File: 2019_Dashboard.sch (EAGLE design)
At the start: 48 parts, among them IC1 MCP23017SO, IC2 MCP23017SO, IC3 MCP23017SO, Y1 16MHz

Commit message: 11/26/18 I2C Dashboard
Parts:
- added LAUNCH, LPADDLE, PARTY1, PARTY2, RPADDLE, T/S-TOOGLE: (no value), SparkFun-Connectors:CONN_02LOCK
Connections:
- new net LAUNCH: IC2.GPB3, LAUNCH.2
- new net LPADDLE: IC2.GPB0, LPADDLE.2
- new net PARTY1: IC2.GPB4, PARTY1.2
- new net PARTY2: IC2.GPB5, PARTY2.2
- new net RPADDLE: IC2.GPB1, RPADDLE.2
- new net T/S-TOOGLE: IC2.GPB2, T/S-TOOGLE.2
- net VCC: now also LAUNCH.1, LPADDLE.1, PARTY1.1, PARTY2.1, RPADDLE.1, T/S-TOOGLE.1
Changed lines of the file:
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@@
 <part name="R12" library="SparkFun-Resistors" library_urn="urn:adsk.eagle:library:532" deviceset="330OHM" device="-0603-1/10W-1%" package3d_urn="urn:adsk.eagle:package:39650/1" value="330"/>
 <part name="GND11" library="SparkFun-PowerSymbols" library_urn="urn:adsk.eagle:library:530" deviceset="GND" device=""/>
+<part name="PARTY2" library="SparkFun-Connectors" library_urn="urn:adsk.eagle:library:513" deviceset="CONN_02" device="LOCK" package3d_urn="urn:adsk.eagle:package:38045/1"/>
+<part name="T/S-TOOGLE" library="SparkFun-Connectors" library_urn="urn:adsk.eagle:library:513" deviceset="CONN_02" device="LOCK" package3d_urn="urn:adsk.eagle:package:38045/1"/>
+<part name="RPADDLE" library="SparkFun-Connectors" library_urn="urn:adsk.eagle:library:513" deviceset="CONN_02" device="LOCK" package3d_urn="urn:adsk.eagle:package:38045/1"/>
+<part name="PARTY1" library="SparkFun-Connectors" library_urn="urn:adsk.eagle:library:513" deviceset="CONN_02" device="LOCK" package3d_urn="urn:adsk.eagle:package:38045/1"/>
+<part name="LAUNCH" library="SparkFun-Connectors" library_urn="urn:adsk.eagle:library:513" deviceset="CONN_02" device="LOCK" package3d_urn="urn:adsk.eagle:package:38045/1"/>
+<part name="LPADDLE" library="SparkFun-Connectors" library_urn="urn:adsk.eagle:library:513" deviceset="CONN_02" device="LOCK" package3d_urn="urn:adsk.eagle:package:38045/1"/>
+<part name="SUPPLY2" library="SparkFun-PowerSymbols" library_urn="urn:adsk.eagle:library:530" deviceset="VCC" device=""/>
+<part name="SUPPLY3" library="SparkFun-PowerSymbols" library_urn="urn:adsk.eagle:library:530" deviceset="VCC" device=""/>
+<part name="SUPPLY4" library="SparkFun-PowerSymbols" library_urn="urn:adsk.eagle:library:530" deviceset="VCC" device=""/>
+<part name="SUPPLY5" library="SparkFun-PowerSymbols" library_urn="urn:adsk.eagle:library:530" deviceset="VCC" device=""/>
+<part name="SUPPLY6" library="SparkFun-PowerSymbols" library_urn="urn:adsk.eagle:library:530" deviceset="VCC" device=""/>
+<part name="SUPPLY7" library="SparkFun-PowerSymbols" library_urn="urn:adsk.eagle:library:530" deviceset="VCC" device=""/>
 </parts>
 <sheets>
@@
 <instance part="R12" gate="G$1" x="78.74" y="-88.9"/>
 <instance part="GND11" gate="1" x="104.14" y="-104.14"/>
+<instance part="PARTY2" gate="G$1" x="-45.72" y="172.72" rot="R180"/>
+<instance part="T/S-TOOGLE" gate="G$1" x="-45.72" y="157.48" rot="R180"/>
+<instance part="RPADDLE" gate="G$1" x="-45.72" y="139.7" rot="R180"/>
+<instance part="PARTY1" gate="G$1" x="-71.12" y="172.72" rot="R180"/>
+<instance part="LAUNCH" gate="G$1" x="-71.12" y="157.48" rot="R180"/>
+<instance part="LPADDLE" gate="G$1" x="-71.12" y="139.7" rot="R180"/>
+<instance part="SUPPLY2" gate="G$1" x="-88.9" y="180.34"/>
+<instance part="SUPPLY3" gate="G$1" x="-60.96" y="182.88"/>
+<instance part="SUPPLY4" gate="G$1" x="-88.9" y="165.1"/>
+<instance part="SUPPLY5" gate="G$1" x="-60.96" y="165.1"/>
+<instance part="SUPPLY6" gate="G$1" x="-60.96" y="147.32"/>
+<instance part="SUPPLY7" gate="G$1" x="-88.9" y="147.32"/>
 </instances>
 <busses>
@@
 <junction x="-15.24" y="129.54"/>
 </segment>
+<segment>
+<pinref part="PARTY1" gate="G$1" pin="1"/>
+<wire x1="-78.74" y1="172.72" x2="-88.9" y2="172.72" width="0.1524" layer="91"/>
+<wire x1="-88.9" y1="172.72" x2="-88.9" y2="180.34" width="0.1524" layer="91"/>
+<pinref part="SUPPLY2" gate="G$1" pin="VCC"/>
+</segment>
+<segment>
+<pinref part="PARTY2" gate="G$1" pin="1"/>
+<wire x1="-53.34" y1="172.72" x2="-60.96" y2="172.72" width="0.1524" layer="91"/>
+<wire x1="-60.96" y1="172.72" x2="-60.96" y2="182.88" width="0.1524" layer="91"/>
+<pinref part="SUPPLY3" gate="G$1" pin="VCC"/>
+</segment>
+<segment>
+<pinref part="LAUNCH" gate="G$1" pin="1"/>
+<wire x1="-78.74" y1="157.48" x2="-88.9" y2="157.48" width="0.1524" layer="91"/>
+<wire x1="-88.9" y1="157.48" x2="-88.9" y2="165.1" width="0.1524" layer="91"/>
+<pinref part="SUPPLY4" gate="G$1" pin="VCC"/>
+</segment>
+<segment>
+<pinref part="T/S-TOOGLE" gate="G$1" pin="1"/>
+<wire x1="-53.34" y1="157.48" x2="-60.96" y2="157.48" width="0.1524" layer="91"/>
+<wire x1="-60.96" y1="157.48" x2="-60.96" y2="165.1" width="0.1524" layer="91"/>
+<pinref part="SUPPLY5" gate="G$1" pin="VCC"/>
+</segment>
+<segment>
+<pinref part="RPADDLE" gate="G$1" pin="1"/>
+<wire x1="-53.34" y1="139.7" x2="-60.96" y2="139.7" width="0.1524" layer="91"/>
+<wire x1="-60.96" y1="139.7" x2="-60.96" y2="147.32" width="0.1524" layer="91"/>
+<pinref part="SUPPLY6" gate="G$1" pin="VCC"/>
+</segment>
+<segment>
+<pinref part="LPADDLE" gate="G$1" pin="1"/>
+<wire x1="-78.74" y1="139.7" x2="-88.9" y2="139.7" width="0.1524" layer="91"/>
+<wire x1="-88.9" y1="139.7" x2="-88.9" y2="147.32" width="0.1524" layer="91"/>
+<pinref part="SUPPLY7" gate="G$1" pin="VCC"/>
+</segment>
 </net>
 <net name="OSC1" class="0">
@@
 </segment>
 </net>
+<net name="RPADDLE" class="0">
+<segment>
+<pinref part="RPADDLE" gate="G$1" pin="2"/>
+<wire x1="-53.34" y1="137.16" x2="-53.34" y2="132.08" width="0.1524" layer="91"/>
+<wire x1="-53.34" y1="132.08" x2="-63.5" y2="132.08" width="0.1524" layer="91"/>
+<label x="-63.5" y="127" size="1.778" layer="95"/>
+</segment>
+<segment>
+<pinref part="IC2" gate="G$1" pin="GPB1"/>
+<wire x1="17.78" y1="45.72" x2="33.02" y2="45.72" width="0.1524" layer="91"/>
+<label x="25.4" y="45.72" size="1.778" layer="95"/>
+</segment>
+</net>
+<net name="LPADDLE" class="0">
+<segment>
+<pinref part="LPADDLE" gate="G$1" pin="2"/>
+<wire x1="-78.74" y1="137.16" x2="-78.74" y2="132.08" width="0.1524" layer="91"/>
+<wire x1="-78.74" y1="132.08" x2="-88.9" y2="132.08" width="0.1524" layer="91"/>
+<label x="-86.36" y="127" size="1.778" layer="95"/>
+</segment>
+<segment>
+<pinref part="IC2" gate="G$1" pin="GPB0"/>
+<wire x1="17.78" y1="48.26" x2="33.02" y2="48.26" width="0.1524" layer="91"/>
+<label x="25.4" y="48.26" size="1.778" layer="95"/>
+</segment>
+</net>
+<net name="LAUNCH" class="0">
+<segment>
+<pinref part="LAUNCH" gate="G$1" pin="2"/>
+<wire x1="-78.74" y1="154.94" x2="-78.74" y2="149.86" width="0.1524" layer="91"/>
+<label x="-81.28" y="149.86" size="1.778" layer="95"/>
+</segment>
+<segment>
+<pinref part="IC2" gate="G$1" pin="GPB3"/>
+<wire x1="17.78" y1="40.64" x2="33.02" y2="40.64" width="0.1524" layer="91"/>
+<label x="25.4" y="40.64" size="1.778" layer="95"/>
+</segment>
+</net>
+<net name="T/S-TOOGLE" class="0">
+<segment>
+<pinref part="T/S-TOOGLE" gate="G$1" pin="2"/>
+<wire x1="-53.34" y1="154.94" x2="-60.96" y2="154.94" width="0.1524" layer="91"/>
+<label x="-58.42" y="160.02" size="1.778" layer="95"/>
+</segment>
+<segment>
+<pinref part="IC2" gate="G$1" pin="GPB2"/>
+<wire x1="17.78" y1="43.18" x2="33.02" y2="43.18" width="0.1524" layer="91"/>
+<label x="25.4" y="43.18" size="1.778" layer="95"/>
+</segment>
+</net>
+<net name="PARTY1" class="0">
+<segment>
+<pinref part="PARTY1" gate="G$1" pin="2"/>
+<wire x1="-78.74" y1="170.18" x2="-86.36" y2="170.18" width="0.1524" layer="91"/>
+<label x="-86.36" y="170.18" size="1.778" layer="95"/>
+</segment>
+<segment>
+<pinref part="IC2" gate="G$1" pin="GPB4"/>
+<wire x1="17.78" y1="38.1" x2="33.02" y2="38.1" width="0.1524" layer="91"/>
+<label x="25.4" y="38.1" size="1.778" layer="95"/>
+</segment>
+</net>
+<net name="PARTY2" class="0">
+<segment>
+<pinref part="PARTY2" gate="G$1" pin="2"/>
+<wire x1="-53.34" y1="170.18" x2="-60.96" y2="170.18" width="0.1524" layer="91"/>
+<label x="-60.96" y="170.18" size="1.778" layer="95"/>
+</segment>
+<segment>
+<pinref part="IC2" gate="G$1" pin="GPB5"/>
+<wire x1="17.78" y1="35.56" x2="35.56" y2="35.56" width="0.1524" layer="91"/>
+<label x="25.4" y="35.56" size="1.778" layer="95"/>
+</segment>
+</net>

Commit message: Yeet a few pins
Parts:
- removed IC2: MCP23017SO, adafruit:MCP23017SO
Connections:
- removed net N$16: IC2.GPA1, U$1.B
- removed net N$17: IC2.GPA2, U$1.C
- removed net N$18: IC2.GPA3, U$1.D
- removed net N$19: IC2.GPA4, U$1.E
- removed net N$20: IC2.GPA5, U$1.F
- removed net N$21: IC2.GPA6, U$1.G
- net GND: now also CONTROL.AGND; no longer IC2.A1, IC2.A2, IC2.VSS, U$1.G2
- net LAUNCH: now also CONTROL.PD5(T1); no longer IC2.GPB3
- net LPADDLE: now also CONTROL.PC1(ADC1); no longer IC2.GPB0
- net N$1: no longer IC2.SCL
- net N$10: now also U$1.DP
- net N$15: now also IC1.GPB4, U$1.G2; no longer IC2.GPA0, U$1.A
- net N$2: no longer IC2.SDA
- net N$3: now also U$1.A
- net N$4: now also U$1.B
- net N$5: now also U$1.C
- net N$6: now also U$1.D
- net N$7: now also U$1.E
- net N$8: now also U$1.F
- net N$9: now also U$1.G
- net PARTY1: now also CONTROL.PD6(AIN0); no longer IC2.GPB4
- net PARTY2: now also CONTROL.PD7(AIN1); no longer IC2.GPB5
- net RPADDLE: now also CONTROL.PC2(ADC2); no longer IC2.GPB1
- net T/S-TOOGLE: now also CONTROL.PC3(ADC3); no longer IC2.GPB2
- net VCC: no longer IC2.!RESET, IC2.A0, IC2.VDD

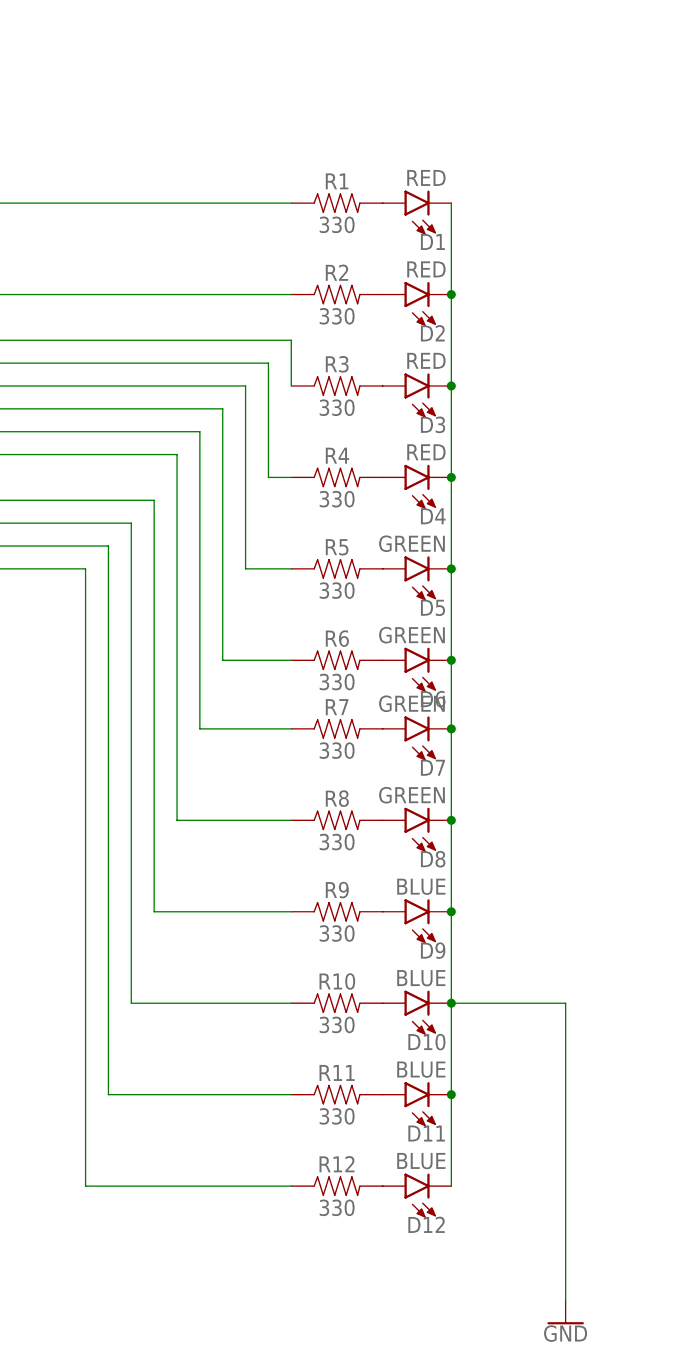
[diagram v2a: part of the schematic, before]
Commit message: Add files via upload
changed LEDs to Through-hole
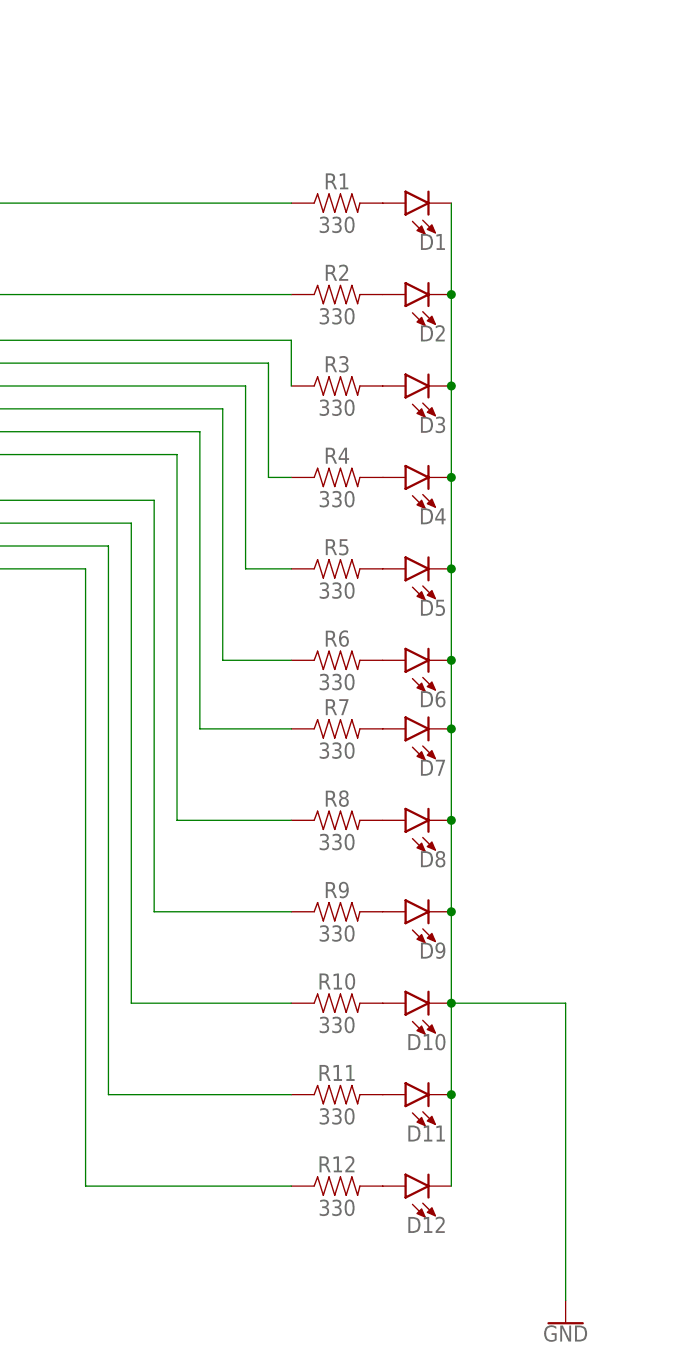
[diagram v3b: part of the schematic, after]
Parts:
- D1, D2, D3, D4: value RED -> (none); device SparkFun-LED:LED-RED1206 -> SparkFun-LED:LED5MM
- D10, D11, D12, D9: value BLUE -> (none); device SparkFun-LED:LED-BLUE1206 -> SparkFun-LED:LED5MM
- D5, D6, D7, D8: value GREEN -> (none); device SparkFun-LED:LED-GREENLILYPAD -> SparkFun-LED:LED5MM
